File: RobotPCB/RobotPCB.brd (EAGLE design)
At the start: 50.8 x 50.8 mm, 42 parts, among them IC1 MPU6050, IC2 MCP73831/OT, U1 DRV8835, U2 CP2104-F03-GM

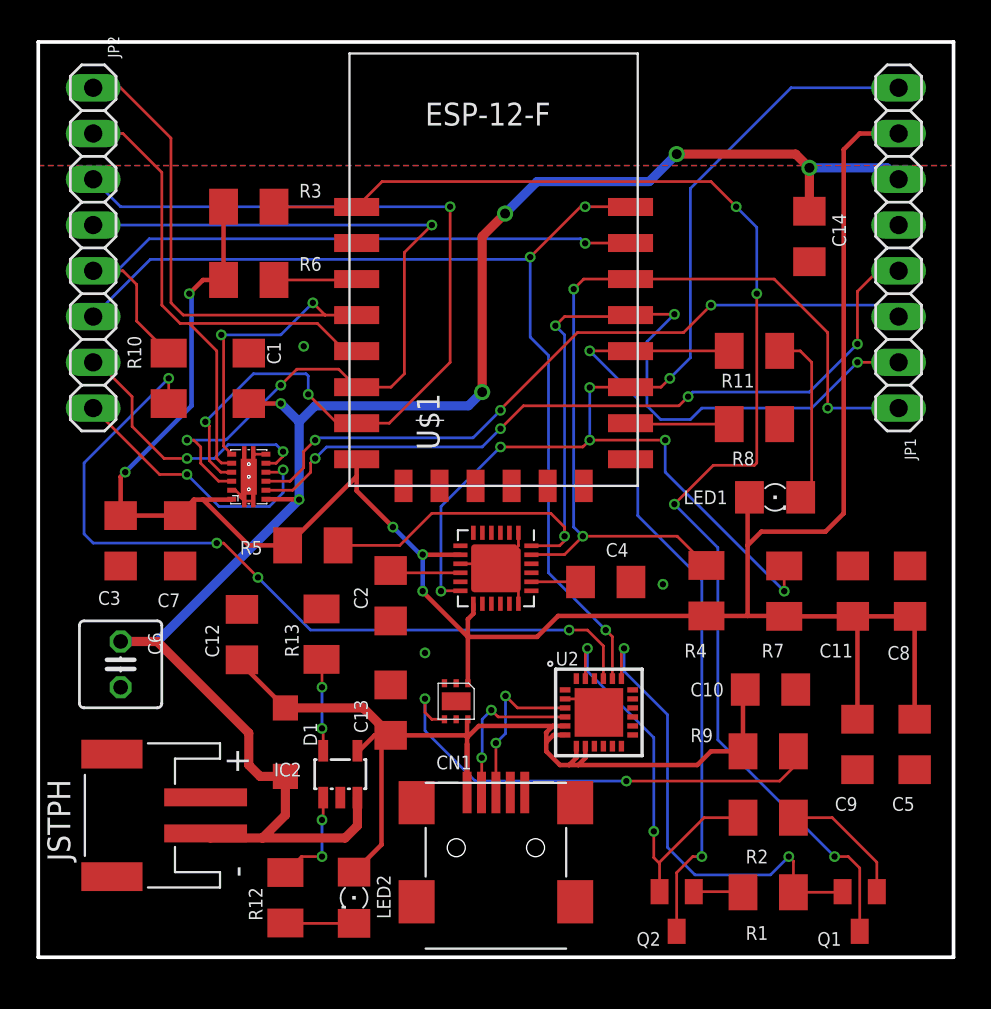
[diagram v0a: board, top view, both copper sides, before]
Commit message: Added text to pins
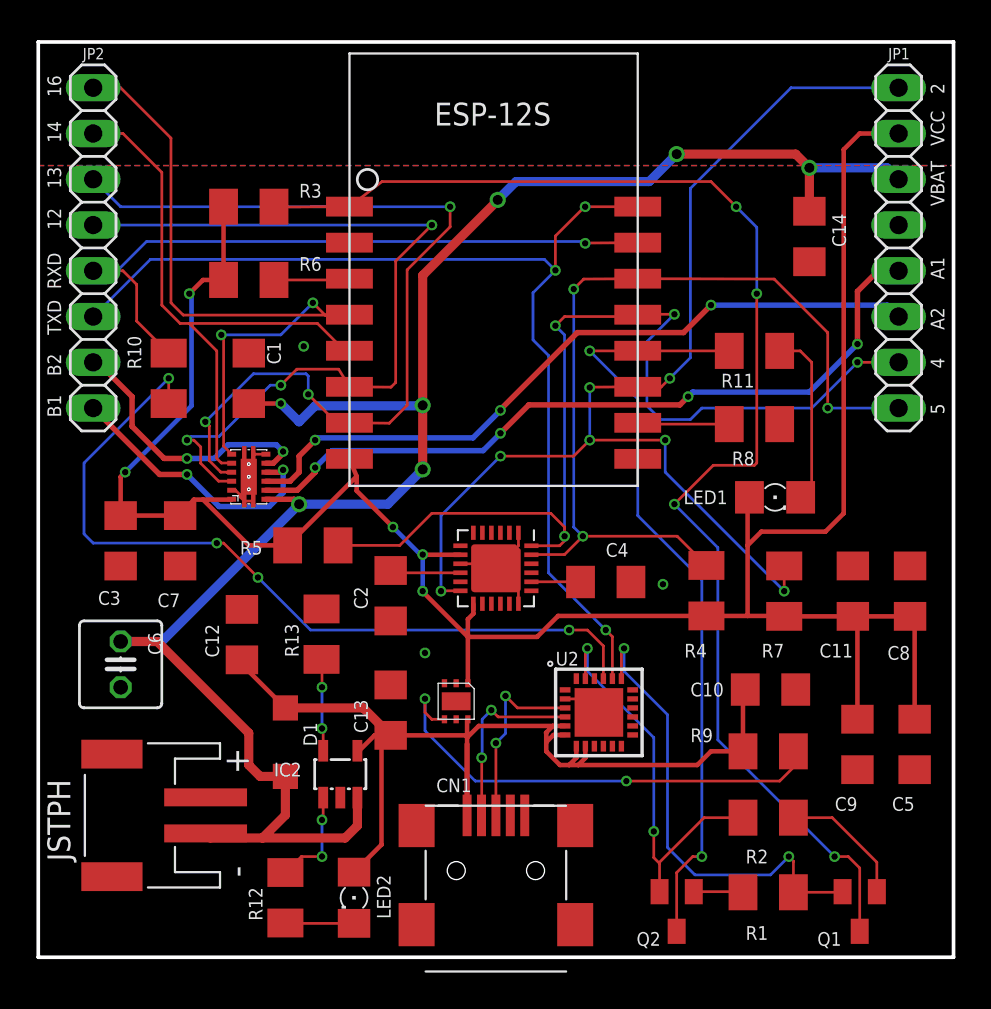
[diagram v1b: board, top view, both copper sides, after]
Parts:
- U$1: device ESP8266-ESP12:ESP8266-ESP12 -> ESP8266:ESP8266-ESP12
- moved CN1 1.27 mm to (25.4, 3.81)
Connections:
- net GND: now also U$1.9; no longer U$1.15
- net GPIO0: now also U$1.12; no longer U$1.18
- net GPIO2: now also U$1.11; no longer U$1.17
- net GPIO4: now also U$1.13; no longer U$1.19
- net GPIO5: now also U$1.14; no longer U$1.20
- net N$23: now also U$1.10; no longer U$1.16
- net RXD: now also U$1.15; no longer U$1.21
- net TXD: now also U$1.16; no longer U$1.22
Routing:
- net VBAT: track 97.6 -> 103.7 mm, vias 6 -> 7
- net TXD: track 57.6 -> 59.4 mm
- net N$7: track 9.05 -> 10.3 mm
- net N$4: track 9.16 -> 10.4 mm
- net VBUS: track 55.1 -> 56.4 mm
- net GPIO0: track 43.4 -> 44.2 mm
- net GPIO4: track 56.4 -> 57.1 mm
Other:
- board text added: "12"
- board text added: "13"
- board text added: "14"
- board text added: "16"
- board text added: "2"
- board text added: "4"
- board text added: "5"
- board text added: "A1"
- board text added: "A2"
- board text added: "B1"
- board text added: "B2"
- board text added: "RXD"
- board text added: "TXD"
- board text added: "VBAT"
- board text added: "VCC"
